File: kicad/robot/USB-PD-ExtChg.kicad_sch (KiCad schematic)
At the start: 18 parts, among them Q3 YJL3416A, Q4 YJL3416A, U18 AP33771DKZ-13

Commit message: bulk BOM edits. Mainly dealing with cap voltage ratings and part selection
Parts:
- C102, C103, C104: Manufacturer (none) -> Samsung; Part Number (none) -> CL10B104KB8NNWC
- C105: Manufacturer (none) -> Samsung; Part Number (none) -> CL10A105KQ8NNNC
- R66: Manufacturer (none) -> N/A; Part Number (none) -> N/A
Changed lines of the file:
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@@
+      (effects (font (size 1.27 1.27)) hide)
+    )
+    (property "Manufacturer" "Samsung" (id 4) (at 298.45 213.36 0)
+      (effects (font (size 1.27 1.27)) hide)
+    )
+    (property "Part Number" "CL10B104KB8NNWC" (id 5) (at 298.45 213.36 0)
       (effects (font (size 1.27 1.27)) hide)
     )
@@
       (effects (font (size 1.27 1.27)) hide)
     )
+    (property "Manufacturer" "Samsung" (id 4) (at 336.55 131.445 0)
+      (effects (font (size 1.27 1.27)) hide)
+    )
+    (property "Part Number" "CL10A105KQ8NNNC" (id 5) (at 336.55 131.445 0)
+      (effects (font (size 1.27 1.27)) hide)
+    )
     (pin "1")
     (pin "2")
@@
     )
     (property "Datasheet" "~" (id 3) (at 316.865 169.545 0)
+      (effects (font (size 1.27 1.27)) hide)
+    )
+    (property "Manufacturer" "Samsung" (id 4) (at 316.865 169.545 0)
+      (effects (font (size 1.27 1.27)) hide)
+    )
+    (property "Part Number" "CL10B104KB8NNWC" (id 5) (at 316.865 169.545 0)
       (effects (font (size 1.27 1.27)) hide)
     )
@@
       (effects (font (size 1.27 1.27)) hide)
     )
+    (property "Manufacturer" "Samsung" (id 4) (at 323.215 194.945 0)
+      (effects (font (size 1.27 1.27)) hide)
+    )
+    (property "Part Number" "CL10B104KB8NNWC" (id 5) (at 323.215 194.945 0)
+      (effects (font (size 1.27 1.27)) hide)
+    )
     (pin "1")
     (pin "2")
@@
       (effects (font (size 1.27 1.27)) hide)
     )
+    (property "Manufacturer" "N/A" (id 4) (at 307.34 129.54 0)
+      (effects (font (size 1.27 1.27)) hide)
+    )
+    (property "Part Number" "N/A" (id 5) (at 307.34 129.54 0)
+      (effects (font (size 1.27 1.27)) hide)
+    )

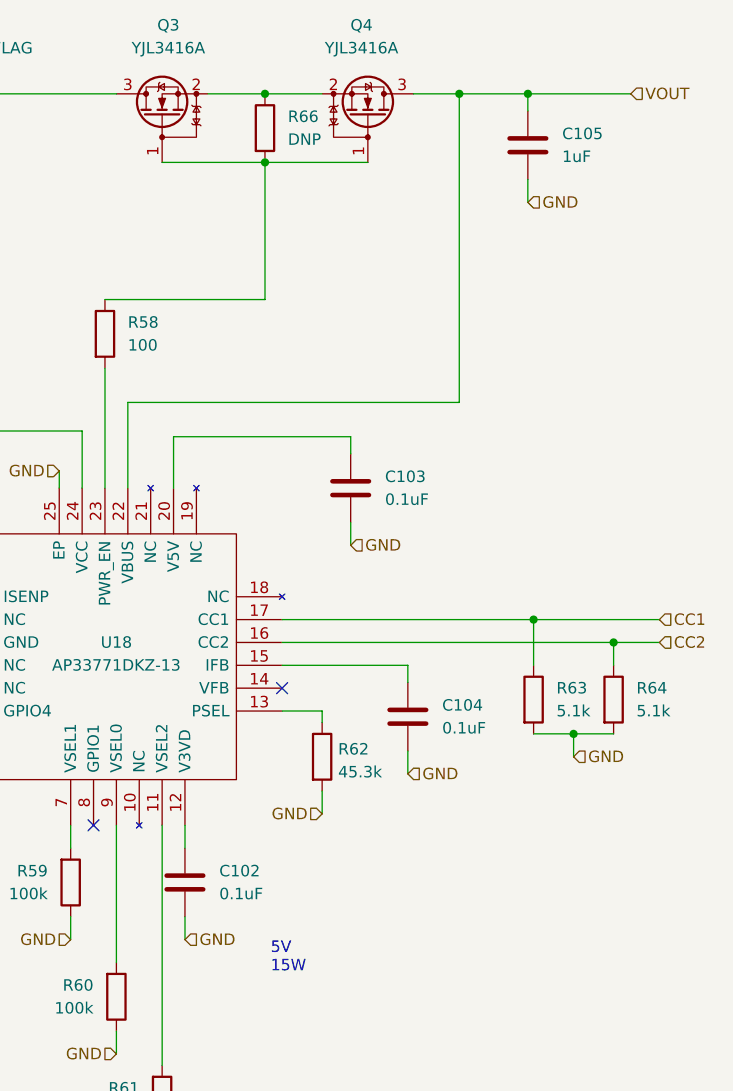
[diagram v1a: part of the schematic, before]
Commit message: Bulk capacitor field edits
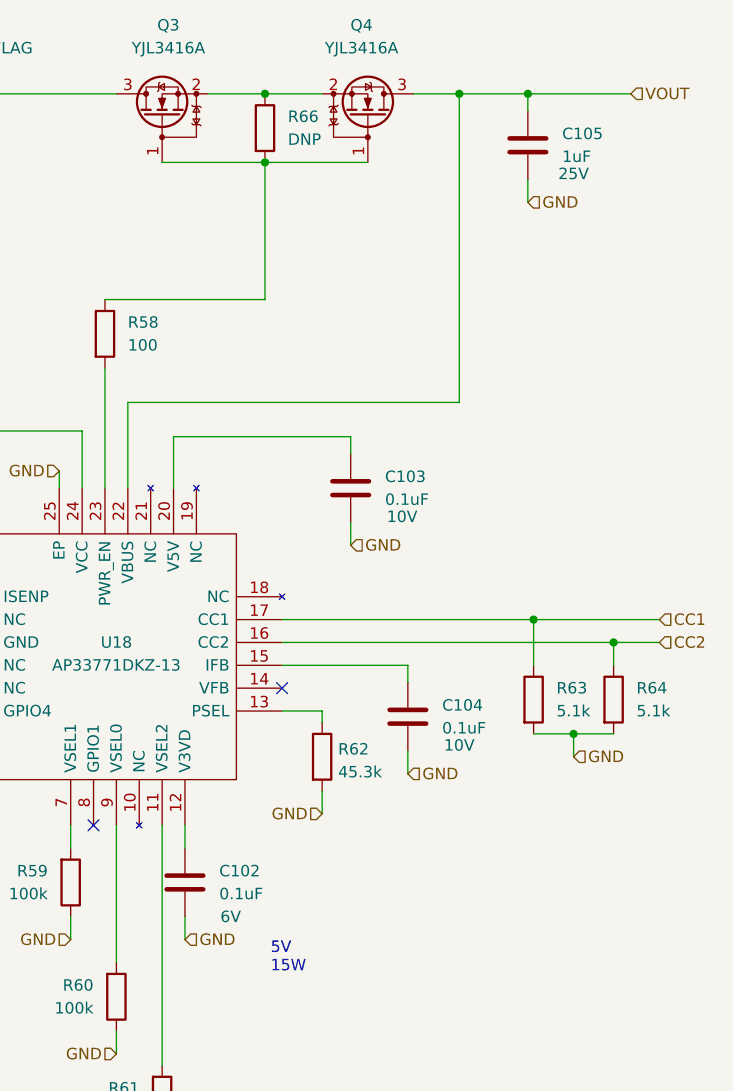
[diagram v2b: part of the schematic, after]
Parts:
- C102, C103, C104: Manufacturer Samsung -> (none); Part Number CL10B104KB8NNWC -> (none)
- C105: Manufacturer Samsung -> (none); Part Number CL10A105KQ8NNNC -> (none)
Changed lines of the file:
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@@
       (effects (font (size 1.27 1.27)) hide)
     )
-    (property "Manufacturer" "Samsung" (id 4) (at 298.45 213.36 0)
-      (effects (font (size 1.27 1.27)) hide)
-    )
-    (property "Part Number" "CL10B104KB8NNWC" (id 5) (at 298.45 213.36 0)
-      (effects (font (size 1.27 1.27)) hide)
-    )
+    (property "Description" "6V" (id 4) (at 303.53 217.17 0))
     (pin "1")
     (pin "2")
@@
       (effects (font (size 1.27 1.27)) hide)
     )
-    (property "Manufacturer" "Samsung" (id 4) (at 336.55 131.445 0)
-      (effects (font (size 1.27 1.27)) hide)
-    )
-    (property "Part Number" "CL10A105KQ8NNNC" (id 5) (at 336.55 131.445 0)
-      (effects (font (size 1.27 1.27)) hide)
-    )
+    (property "Description" "25V" (id 4) (at 341.63 134.62 0))
     (pin "1")
     (pin "2")
@@
       (effects (font (size 1.27 1.27)) hide)
     )
-    (property "Manufacturer" "Samsung" (id 4) (at 316.865 169.545 0)
-      (effects (font (size 1.27 1.27)) hide)
-    )
-    (property "Part Number" "CL10B104KB8NNWC" (id 5) (at 316.865 169.545 0)
-      (effects (font (size 1.27 1.27)) hide)
-    )
+    (property "Description" "10V" (id 4) (at 322.58 172.72 0))
     (pin "1")
     (pin "2")
@@
       (effects (font (size 1.27 1.27)) hide)
     )
-    (property "Manufacturer" "Samsung" (id 4) (at 323.215 194.945 0)
-      (effects (font (size 1.27 1.27)) hide)
-    )
-    (property "Part Number" "CL10B104KB8NNWC" (id 5) (at 323.215 194.945 0)
-      (effects (font (size 1.27 1.27)) hide)
-    )
-    (pin "1")
-    (pin "2")
+    (property "Description" "10V" (id 4) (at 328.93 198.12 0))
+    (pin "1")
+    (pin "2")

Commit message: bulk footprint updates to capacitors
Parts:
- C102, C103, C104, C105: footprint Capacitor_SMD:C_0603_1608Metric -> Capacitor_SMD:C_0402_1005Metric
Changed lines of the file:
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@@
       (effects (font (size 1.27 1.27)) (justify left))
     )
-    (property "Footprint" "Capacitor_SMD:C_0603_1608Metric" (id 2) (at 299.4152 217.17 0)
+    (property "Footprint" "Capacitor_SMD:C_0402_1005Metric" (id 2) (at 299.4152 217.17 0)
       (effects (font (size 1.27 1.27)) hide)
     )
@@
       (effects (font (size 1.27 1.27)) (justify left))
     )
-    (property "Footprint" "Capacitor_SMD:C_0603_1608Metric" (id 2) (at 337.5152 135.255 0)
+    (property "Footprint" "Capacitor_SMD:C_0402_1005Metric" (id 2) (at 337.5152 135.255 0)
       (effects (font (size 1.27 1.27)) hide)
     )
@@
       (effects (font (size 1.27 1.27)) (justify left))
     )
-    (property "Footprint" "Capacitor_SMD:C_0603_1608Metric" (id 2) (at 317.8302 173.355 0)
+    (property "Footprint" "Capacitor_SMD:C_0402_1005Metric" (id 2) (at 317.8302 173.355 0)
       (effects (font (size 1.27 1.27)) hide)
     )
@@
       (effects (font (size 1.27 1.27)) (justify left))
     )
-    (property "Footprint" "Capacitor_SMD:C_0603_1608Metric" (id 2) (at 324.1802 198.755 0)
-      (effects (font (size 1.27 1.27)) hide)
-    )
+    (property "Footprint" "Capacitor_SMD:C_0402_1005Metric" (id 2) (at 324.1802 198.755 0)
+      (effects (font (size 1.27 1.27)) hide)
+    )

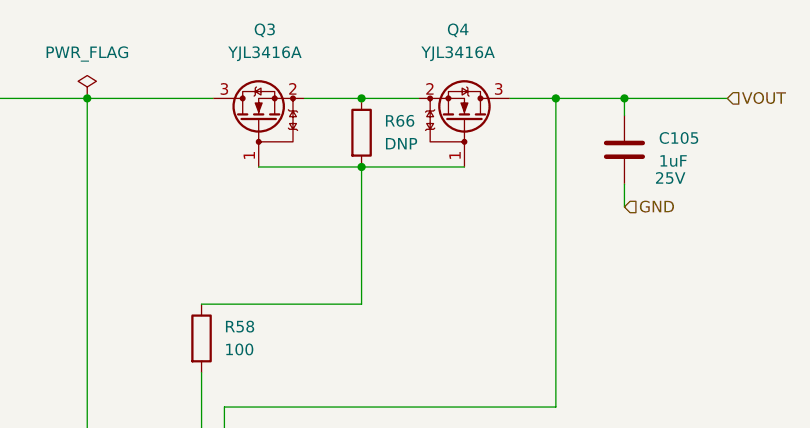
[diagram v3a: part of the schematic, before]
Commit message: R66 to 10k
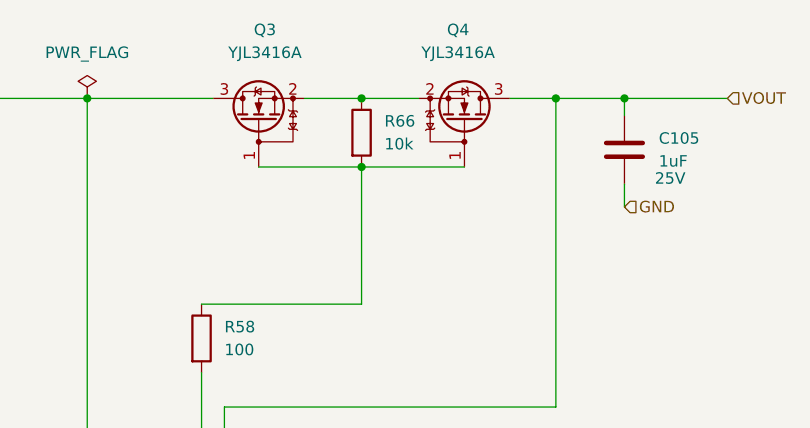
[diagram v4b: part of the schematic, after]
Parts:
- R66: value DNP -> 10k
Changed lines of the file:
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@@
       (effects (font (size 1.27 1.27)) (justify left))
     )
-    (property "Value" "DNP" (id 1) (at 309.88 130.8099 0)
+    (property "Value" "10k" (id 1) (at 309.88 130.8099 0)
       (effects (font (size 1.27 1.27)) (justify left))
     )

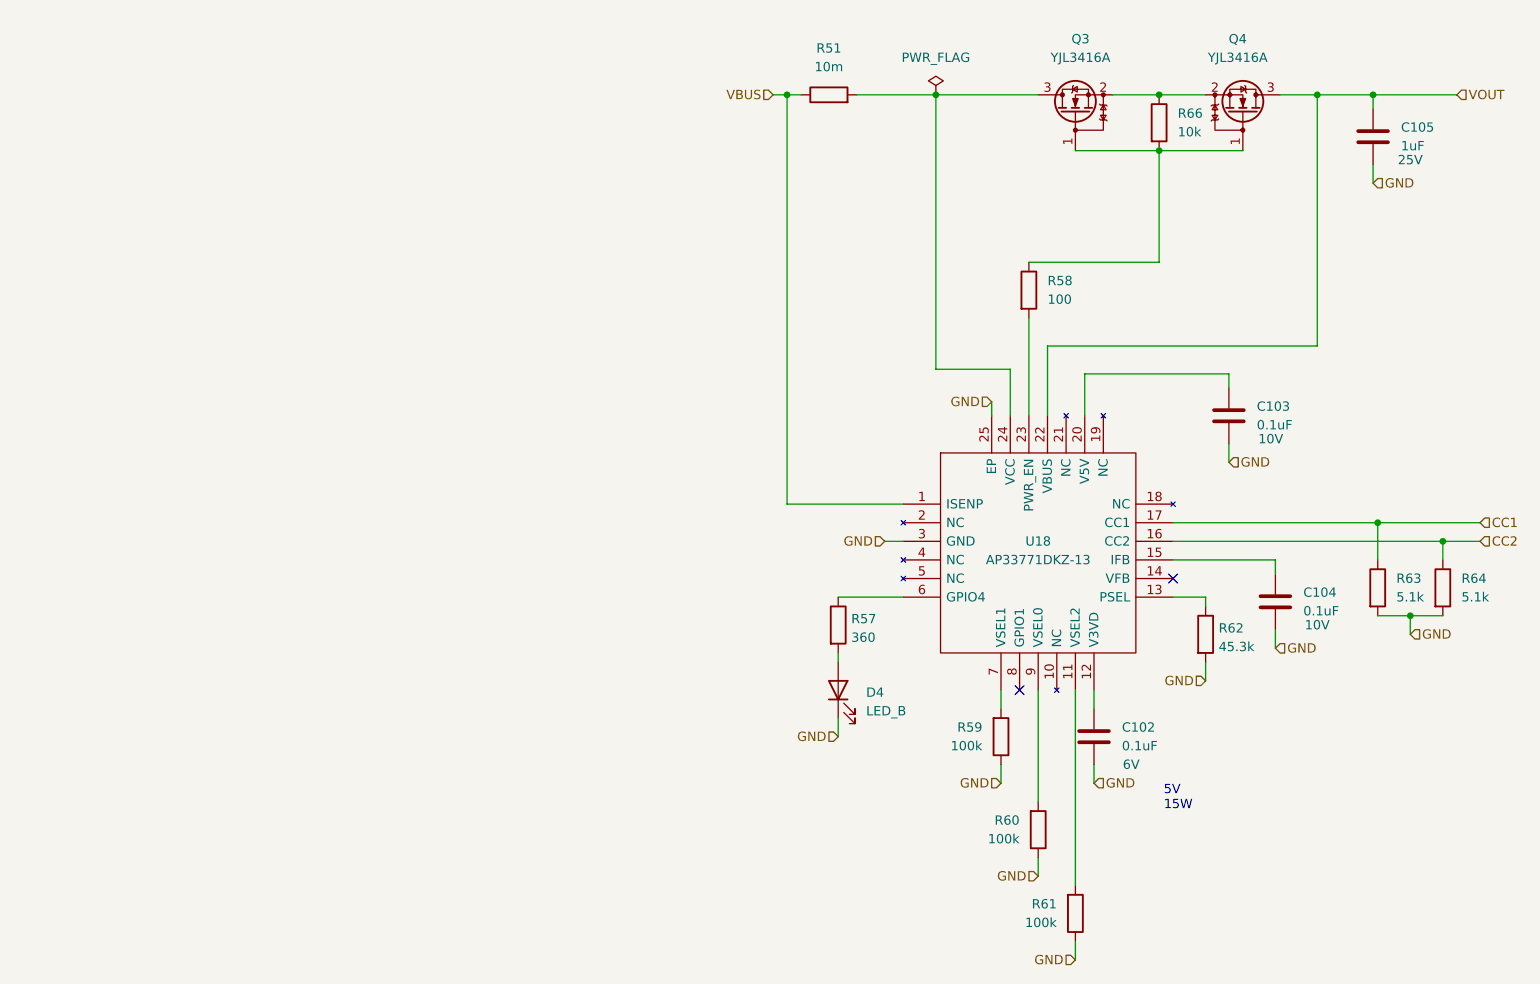
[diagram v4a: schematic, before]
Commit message: Moved USB connector into USB-PD-ExtChg sheet
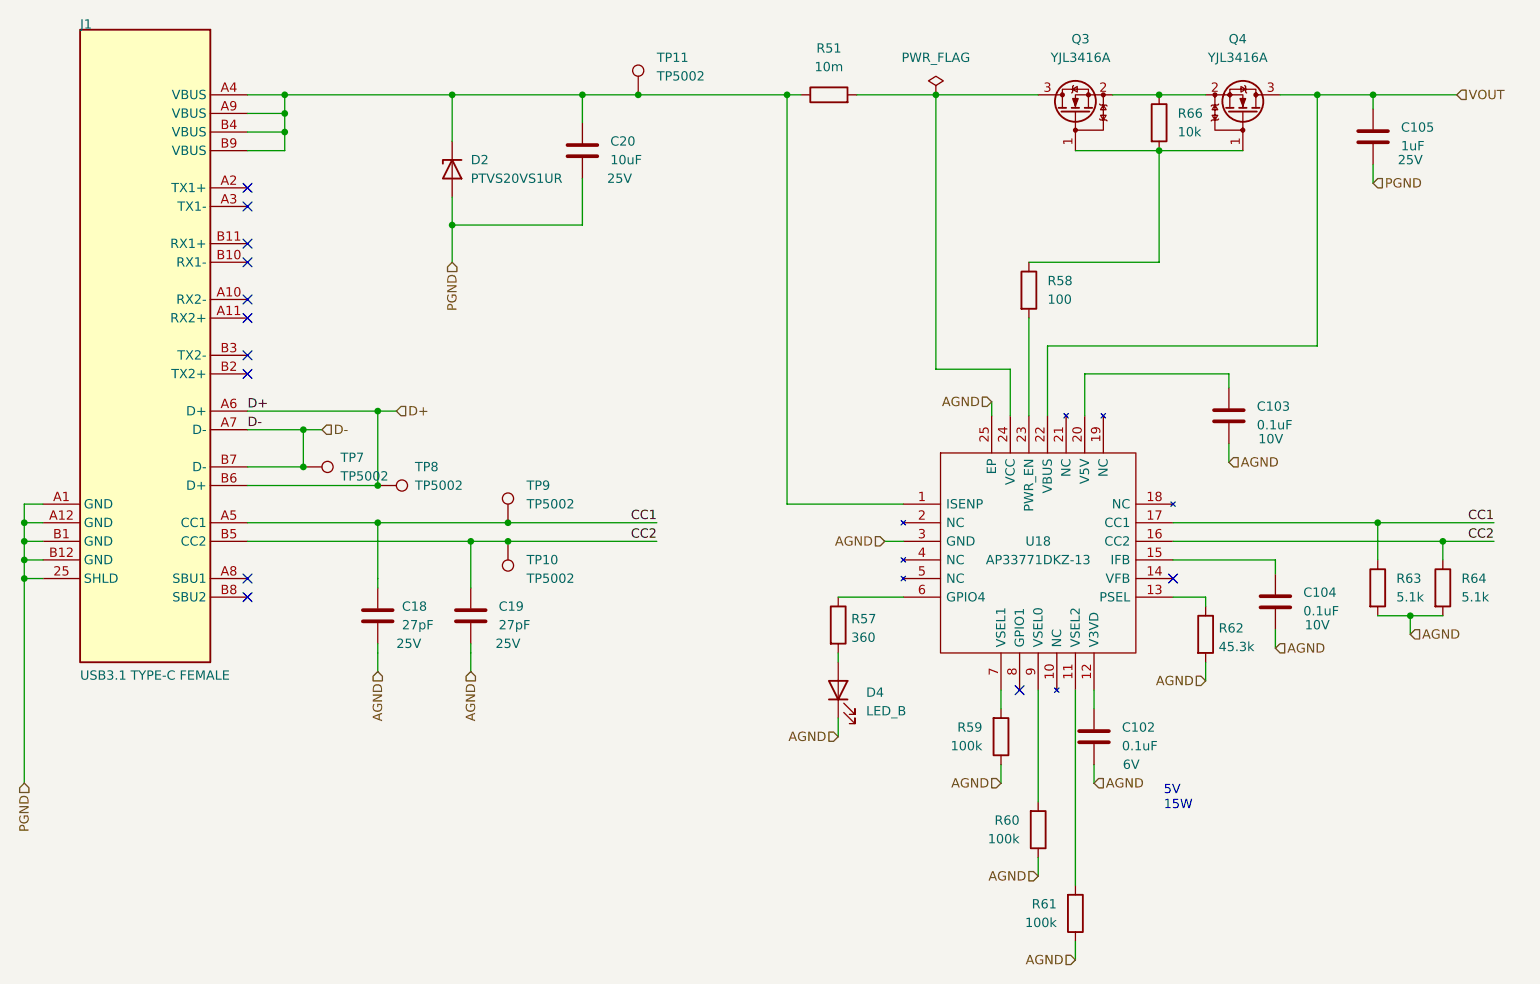
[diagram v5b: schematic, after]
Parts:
- added C18, C19: 27pF, Capacitor_SMD:C_0402_1005Metric, symbol Device:C
- added C20: 10uF, Capacitor_SMD:C_0603_1608Metric, symbol Device:C
- added D2: PTVS20VS1UR, Diode_SMD:Nexperia_CFP3_SOD-123W, symbol Device:D_Zener
- added J1: USBC_Receptacle_SMD_RA, AltiumImports:CON_USB3.1-C_RCPT_SMD_RA_ACP_12401610E4#2A, symbol Connector:0_mirrored_USBC_Receptacle_SMD_RA
- added TP10, TP11, TP7, TP8, TP9: TP5002, TestPoint:KEYSTONE_5002, symbol Connector:TestPoint
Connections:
- net CC1: now also C18.1, J1.A5 (CC1), TP9.1
- net CC2: now also C19.1, J1.B5 (CC2), TP10.1
- net GND renamed AGND
- net AGND: now also C18.2, C19.2; no longer C105.2
- net VBUS: no longer names the net of R51.1, U18.1 (ISENP)
- net VBUS: now also C20.1, D2.1 (K), J1.A4 (VBUS), J1.A9 (VBUS), J1.B4 (VBUS), J1.B9 (VBUS), TP11.1
- new net D+: J1.A6 (D+), J1.B6 (D+), TP8.1
- new net D-: J1.A7 (D-), J1.B7 (D-), TP7.1
- new net PGND: C105.2, C20.2, D2.2 (A), J1.25 (SHLD), J1.A1 (GND), J1.A12 (GND), J1.B1 (GND), J1.B12 (GND)
- no-connect marks 2 -> 12
